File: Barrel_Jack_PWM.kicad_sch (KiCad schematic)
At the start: 18 parts, among them J28 Barrel_Jack_Switch_Pin3Ring, J29 Barrel_Jack_Switch_Pin3Ring, J30 Barrel_Jack_Switch_Pin3Ring, J31 Barrel_Jack_Switch_Pin3Ring, J32 Barrel_Jack_Switch_Pin3Ring, J33 Barrel_Jack_Switch_Pin3Ring, J34 Barrel_Jack_Switch_Pin3Ring, J35 Barrel_Jack_Switch_Pin3Ring, U36 PCA9685PW

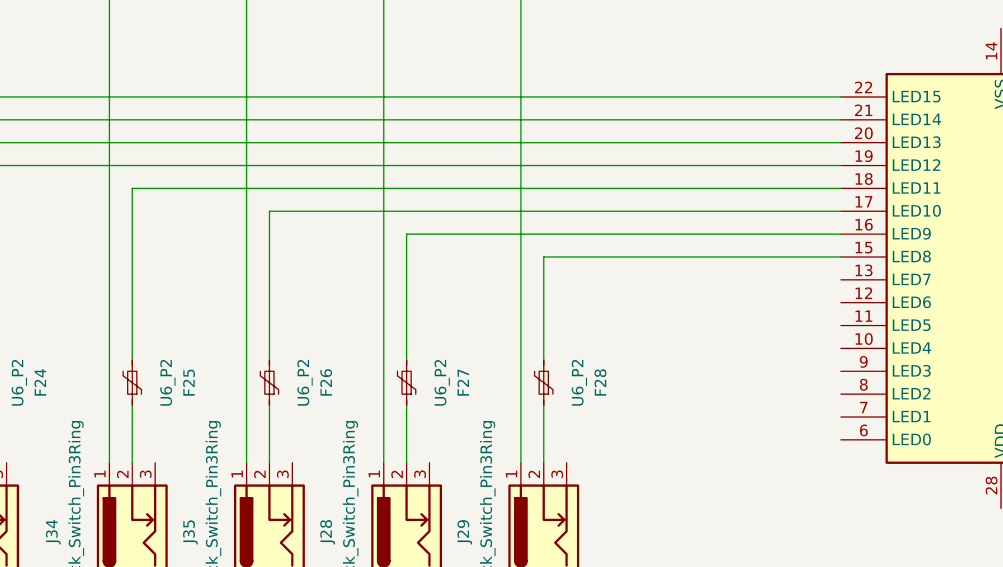
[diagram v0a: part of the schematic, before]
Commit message: add level converter to be compatible with high volt relay
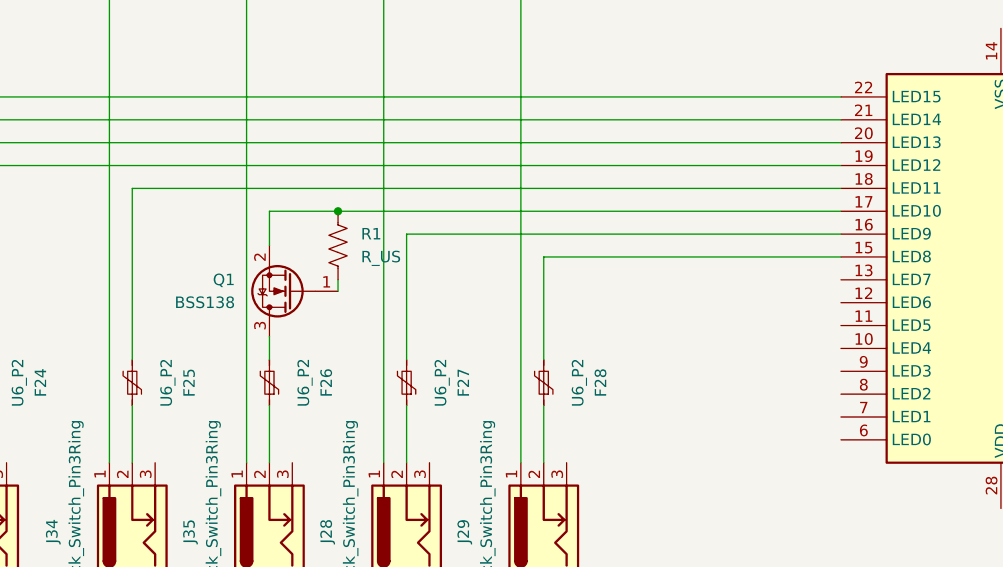
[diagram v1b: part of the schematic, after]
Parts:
- added Q1: BSS138, Package_TO_SOT_SMD:SOT-23, symbol Transistor_FET:BSS138
- added R1: R_US, symbol Device:R_US
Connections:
- net at U36.17 (LED10): now also Q1.2 (S), R1.1; no longer F26.2
- new net: Q1.1 (G), R1.2
- new net: F26.2, Q1.3 (D)
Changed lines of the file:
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@@
   (junction (at 83.82 24.13) (diameter 0) (color 0 0 0 0)
   )
+  (junction (at 140.97 116.84) (diameter 0) (color 0 0 0 0)
+  )
   (junction (at 115.57 24.13) (diameter 0) (color 0 0 0 0)
   )
@@
   (junction (at 146.05 24.13) (diameter 0) (color 0 0 0 0)
   )
-  (wire (pts (xy 133.35 116.84) (xy 133.35 133.35))
+  (wire (pts (xy 133.35 116.84) (xy 133.35 120.65))
     (stroke (width 0) (type default))
   )
@@
     (stroke (width 0) (type default))
   )
+  (wire (pts (xy 140.97 124.46) (xy 140.97 125.73))
+    (stroke (width 0) (type default))
+  )
   (wire (pts (xy 71.12 138.43) (xy 71.12 144.78))
     (stroke (width 0) (type default))
@@
     (stroke (width 0) (type default))
   )
+  (wire (pts (xy 133.35 130.81) (xy 133.35 133.35))
+    (stroke (width 0) (type default))
+  )
   (wire (pts (xy 148.59 119.38) (xy 148.59 133.35))
     (stroke (width 0) (type default))
@@
     (stroke (width 0) (type default))
   )
+  (wire (pts (xy 140.97 116.84) (xy 196.85 116.84))
+    (stroke (width 0) (type default))
+  )
   (wire (pts (xy 99.06 24.13) (xy 99.06 144.78))
     (stroke (width 0) (type default))
@@
     (stroke (width 0) (type default))
   )
-  (wire (pts (xy 133.35 116.84) (xy 196.85 116.84))
+  (wire (pts (xy 133.35 116.84) (xy 140.97 116.84))
     (stroke (width 0) (type default))
   )
@@
         (path "/dab6683c-420f-459a-bf9c-0c28b4b081e3/d534b787-d3bc-419e-b481-23d8b9503201/1cc14268-3ddf-43de-8fc4-aa3fdc953b28"
           (reference "J35") (unit 1)
+        )
+      )
+    )
+  )
+  (symbol (lib_id "Transistor_FET:BSS138") (at 135.89 125.73 180) (unit 1)
+    (in_bom yes) (on_board yes) (dnp no) (fields_autoplaced)
+    (property "Reference" "Q1" (at 129.54 124.46 0)
+      (effects (font (size 1.27 1.27)) (justify left))
+    )
+    (property "Value" "BSS138" (at 129.54 127 0)
+      (effects (font (size 1.27 1.27)) (justify left))
+    )
+    (property "Footprint" "Package_TO_SOT_SMD:SOT-23" (at 130.81 123.825 0)
+      (effects (font (size 1.27 1.27) italic) (justify left) hide)
+    )
+    (property "Datasheet" "https://www.onsemi.com/pub/Collateral/BSS138-D.PDF" (at 130.81 121.92 0)
+      (effects (font (size 1.27 1.27)) (justify left) hide)
+    )
+    (pin "3")
+    (pin "1")
+    (pin "2")
+    (instances
+      (project "esp"
+        (path "/dab6683c-420f-459a-bf9c-0c28b4b081e3/d534b787-d3bc-419e-b481-23d8b9503201/1cc14268-3ddf-43de-8fc4-aa3fdc953b28"
+          (reference "Q1") (unit 1)
         )
       )
@@
         )
       )
+    )
+  )
+  (symbol (lib_id "Device:R_US") (at 140.97 120.65 0) (unit 1)
+    (in_bom yes) (on_board yes) (dnp no) (fields_autoplaced)
+    (property "Reference" "R1" (at 143.51 119.38 0)
+      (effects (font (size 1.27 1.27)) (justify left))
+    )
+    (property "Value" "R_US" (at 143.51 121.92 0)
+      (effects (font (size 1.27 1.27)) (justify left))
+    )
+    (property "Footprint" "" (at 141.986 120.904 90)
+      (effects (font (size 1.27 1.27)) hide)
+    )
+    (property "Datasheet" "~" (at 140.97 120.65 0)
+      (effects (font (size 1.27 1.27)) hide)
+    )
+    (pin "1")
+    (pin "2")
+    (instances
+      (project "esp"
+        (path "/dab6683c-420f-459a-bf9c-0c28b4b081e3/d534b787-d3bc-419e-b481-23d8b9503201/1cc14268-3ddf-43de-8fc4-aa3fdc953b28"
+          (reference "R1") (unit 1)
+        )
+      )

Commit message: slimmed down and spread out pcb
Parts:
- removed BT3: Battery, symbol Device:Battery
- removed F21, F22, F23, F24, F25, F26, F27, F28: U6_P2, symbol Device:Polyfuse_Small
- removed J28, J29, J30, J31, J32, J33, J34, J35: Barrel_Jack_Switch_Pin3Ring, symbol Connector:Barrel_Jack_Switch_Pin3Ring
- removed Q1: BSS138, Package_TO_SOT_SMD:SOT-23, symbol Transistor_FET:BSS138
- removed R1: R_US, symbol Device:R_US
- removed U36: PCA9685PW, Package_SO:TSSOP-28_4.4x9.7mm_P0.65mm, symbol Driver_LED:PCA9685PW
